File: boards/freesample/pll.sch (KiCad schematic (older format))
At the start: 36 parts, among them J13 SMA, J14 SMA, J22 SMA, J23 SMA, U14 LMK04806, U15 ASG-D-V-A-125.000MHZ

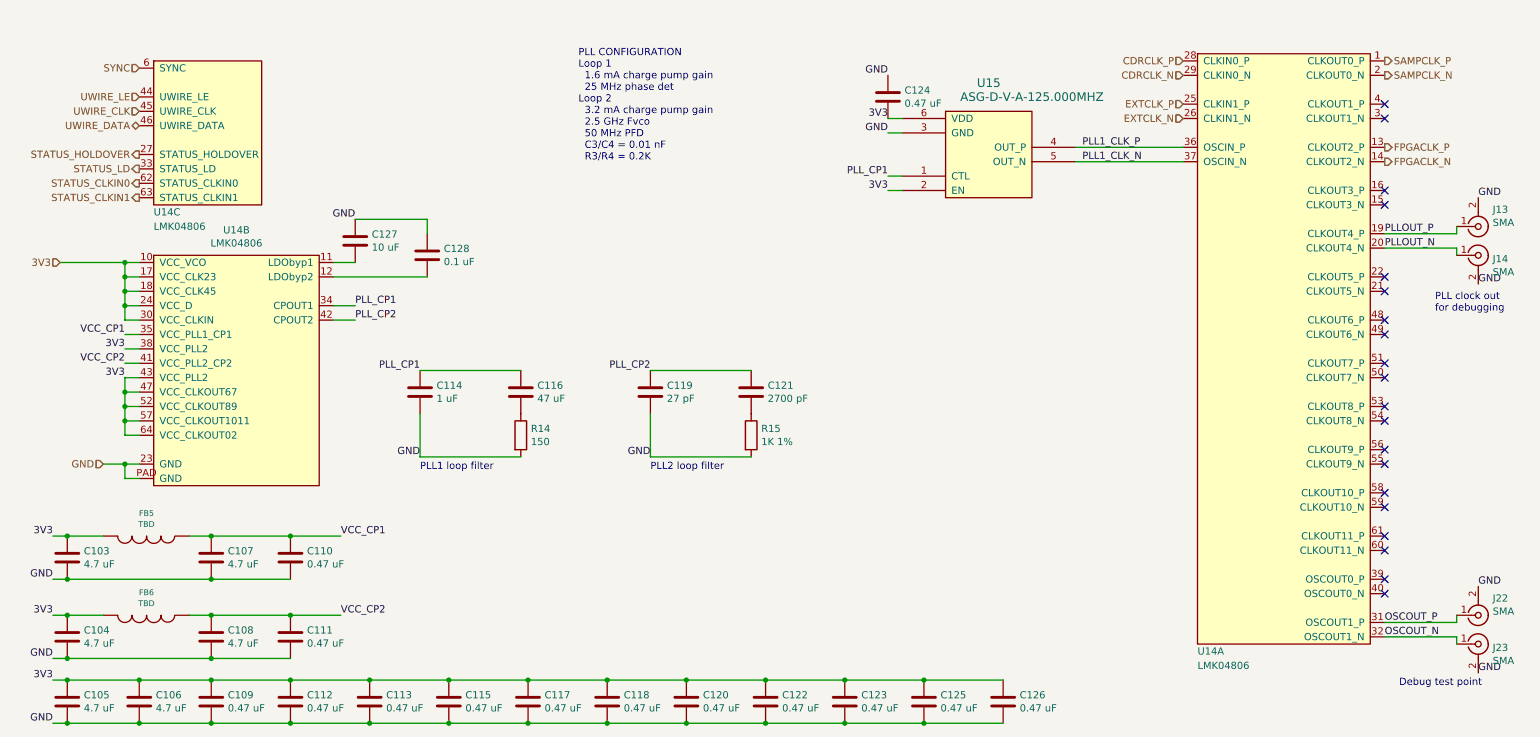
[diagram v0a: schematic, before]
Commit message: Added more test points. Started picking packages for passives. Continued schematic review.
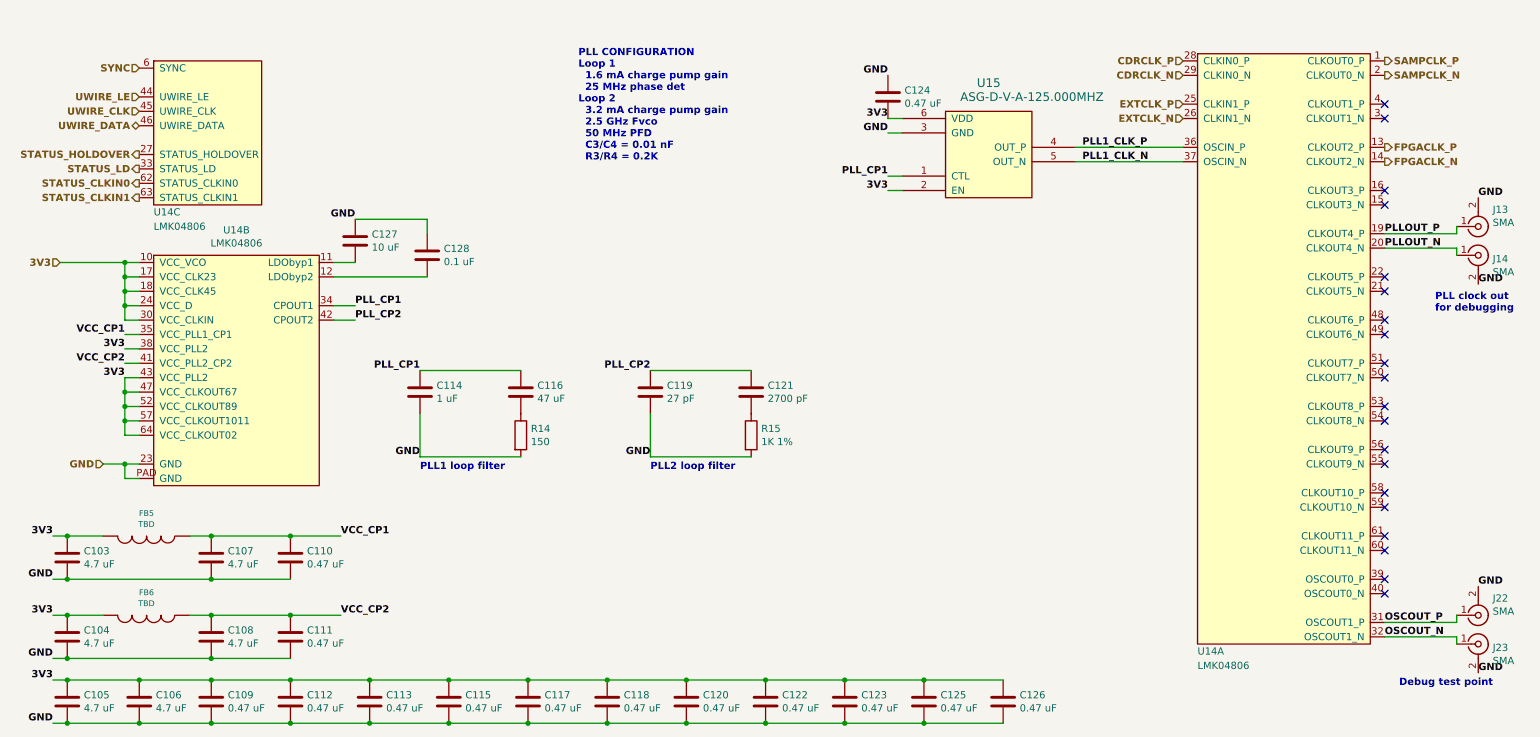
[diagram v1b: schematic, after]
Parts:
- C103, C104, C105, C106, C107, C108: footprint (none) -> azonenberg_pcb:EIA_0603_CAP_NOSILK
- C109, C110, C111, C112, C113, C114, C115, C117, C118, C119, C120, C121, C122, C123, C124, C125, C126, C128: footprint (none) -> azonenberg_pcb:EIA_0402_CAP_NOSILK
- C116: footprint (none) -> azonenberg_pcb:EIA_1210_CAP_NOSILK
- C127: footprint (none) -> azonenberg_pcb:EIA_1206_CAP_NOSILK
- J13, J14, J22, J23: footprint (none) -> azonenberg_pcb:CONN_SMA_EDGE_SAMTEC_SMA_J_P_H_ST_EM1
- U14: footprint (none) -> azonenberg_pcb:QFN_64_0.5MM_9x9MM

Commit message: Continued assigning footprints
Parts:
- FB5, FB6: value TBD -> BLM15PX121SN1D; footprint (none) -> azonenberg_pcb:EIA_0402_CAP_NOSILK
- R14, R15: footprint (none) -> azonenberg_pcb:EIA_0402_RES_NOSILK
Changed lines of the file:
@@
 Sheet 5 12
 Title "FREESAMPLE Oscilloscope"
-Date "2019-03-15"
+Date "2019-03-16"
 Rev "0.1"
 Comp "Andrew D. Zonenberg / Antikernel Labs"
@@
 P 1650 4250
 F 0 "FB5" V 1492 4250 40  0000 C CNN
-F 1 "TBD" V 1568 4250 40  0000 C CNN
-F 2 "" H 1650 4250 60  0001 C CNN
+F 1 "BLM15PX121SN1D" V 1568 4250 40  0000 C CNN
+F 2 "azonenberg_pcb:EIA_0402_CAP_NOSILK" H 1650 4250 60  0001 C CNN
 F 3 "" H 1650 4250 60  0000 C CNN
 	1    1650 4250
@@
 P 1650 4800
 F 0 "FB6" V 1492 4800 40  0000 C CNN
-F 1 "TBD" V 1568 4800 40  0000 C CNN
-F 2 "" H 1650 4800 60  0001 C CNN
+F 1 "BLM15PX121SN1D" V 1568 4800 40  0000 C CNN
+F 2 "azonenberg_pcb:EIA_0402_CAP_NOSILK" H 1650 4800 60  0001 C CNN
 F 3 "" H 1650 4800 60  0000 C CNN
 	1    1650 4800
@@
 F 0 "R14" H 4320 3596 50  0000 L CNN
 F 1 "150" H 4320 3505 50  0000 L CNN
-F 2 "" V 4180 3550 50  0001 C CNN
+F 2 "azonenberg_pcb:EIA_0402_RES_NOSILK" V 4180 3550 50  0001 C CNN
 F 3 "" H 4250 3550 50  0001 C CNN
 	1    4250 3550
@@
 F 0 "R15" H 5920 3596 50  0000 L CNN
 F 1 "1K 1%" H 5920 3505 50  0000 L CNN
-F 2 "" V 5780 3550 50  0001 C CNN
+F 2 "azonenberg_pcb:EIA_0402_RES_NOSILK" V 5780 3550 50  0001 C CNN
 F 3 "" H 5850 3550 50  0001 C CNN
 	1    5850 3550

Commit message: Added fiducials
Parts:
- U15: footprint (none) -> azonenberg_pcb:VCXO_5x7MM_ASG_D
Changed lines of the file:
@@
 F 0 "U15" H 7500 2697 60  0000 C CNN
 F 1 "ASG-D-V-A-125.000MHZ" H 7800 2600 60  0000 C CNN
-F 2 "" H 7200 1900 60  0001 C CNN
+F 2 "azonenberg_pcb:VCXO_5x7MM_ASG_D" H 7200 1900 60  0001 C CNN
 F 3 "" H 7200 1900 60  0000 C CNN
 	1    7200 1900

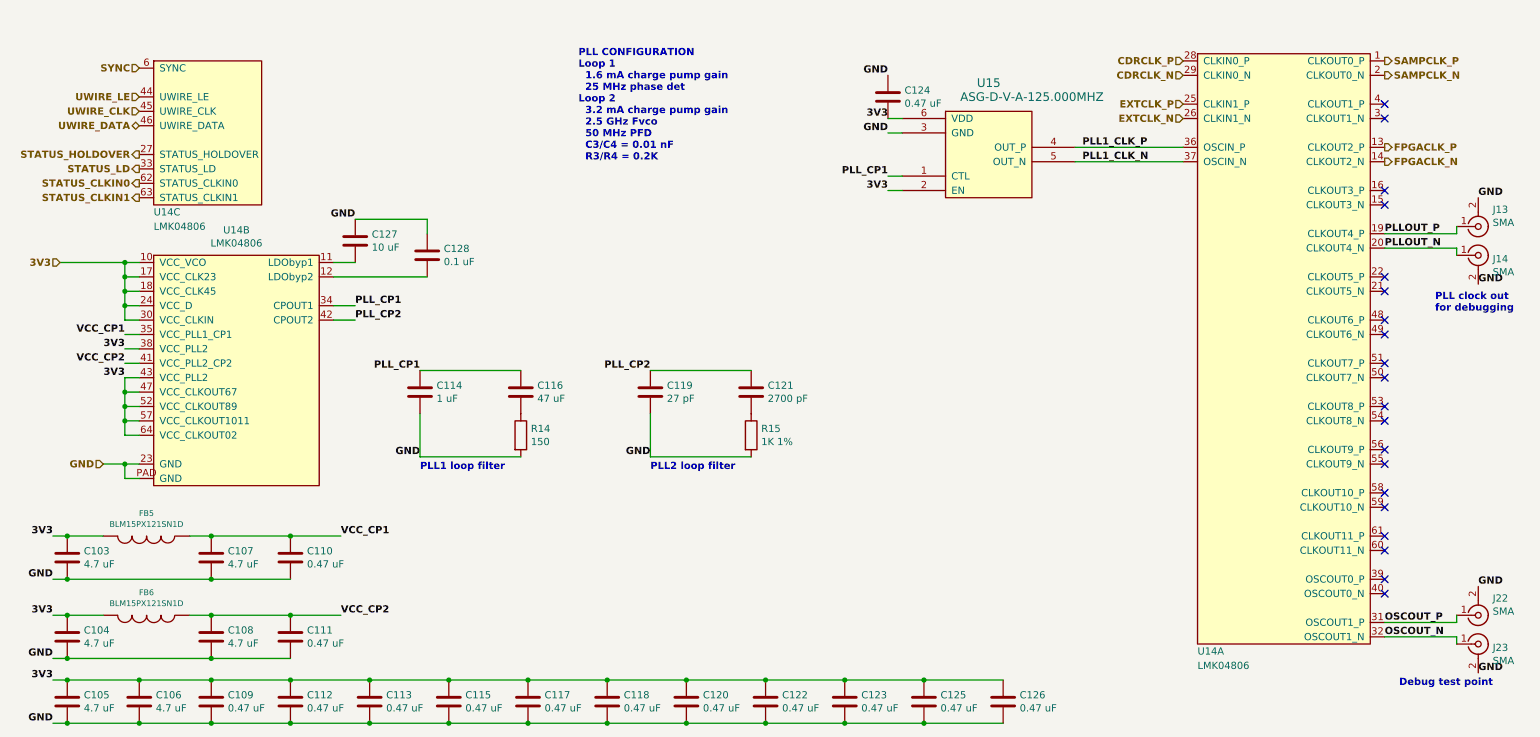
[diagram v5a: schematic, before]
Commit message: Began layout on clock recovery block
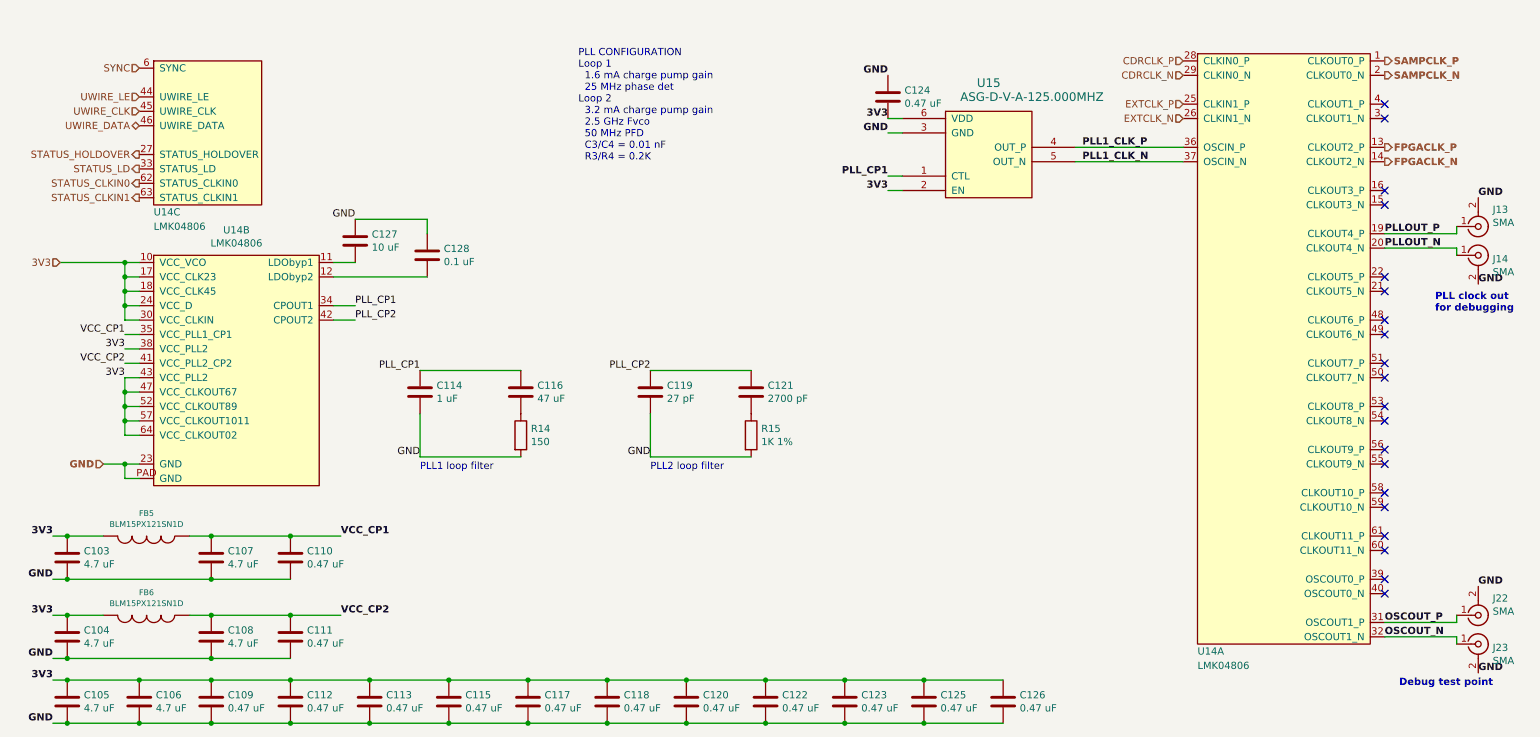
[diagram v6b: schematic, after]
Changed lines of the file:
@@
 Comment4 ""
 $EndDescr
-Text HLabel 8850 950  0    50   Input ~ 10
+Text HLabel 8850 950  0    50   Input ~ 0
 CDRCLK_P
-Text HLabel 8850 1050 0    50   Input ~ 10
+Text HLabel 8850 1050 0    50   Input ~ 0
 CDRCLK_N
-Text HLabel 8850 1250 0    50   Input ~ 10
+Text HLabel 8850 1250 0    50   Input ~ 0
 EXTCLK_P
-Text HLabel 8850 1350 0    50   Input ~ 10
+Text HLabel 8850 1350 0    50   Input ~ 0
 EXTCLK_N
-Text HLabel 1050 2350 0    50   Input ~ 10
+Text HLabel 1050 2350 0    50   Input ~ 0
 3V3
 Text HLabel 1350 3750 0    50   Input ~ 10
@@
 Text HLabel 10250 1050 2    50   Output ~ 10
 SAMPCLK_N
-Text HLabel 1600 1000 0    50   Input ~ 10
+Text HLabel 1600 1000 0    50   Input ~ 0
 SYNC
-Text HLabel 1600 1600 0    50   Output ~ 10
+Text HLabel 1600 1600 0    50   Output ~ 0
 STATUS_HOLDOVER
-Text HLabel 1600 1700 0    50   Output ~ 10
+Text HLabel 1600 1700 0    50   Output ~ 0
 STATUS_LD
-Text HLabel 1600 1200 0    50   Input ~ 10
+Text HLabel 1600 1200 0    50   Input ~ 0
 UWIRE_LE
-Text HLabel 1600 1300 0    50   Input ~ 10
+Text HLabel 1600 1300 0    50   Input ~ 0
 UWIRE_CLK
-Text HLabel 1600 1400 0    50   BiDi ~ 10
+Text HLabel 1600 1400 0    50   BiDi ~ 0
 UWIRE_DATA
-Text HLabel 1600 1800 0    50   Output ~ 10
+Text HLabel 1600 1800 0    50   Output ~ 0
 STATUS_CLKIN0
-Text HLabel 1600 1900 0    50   Output ~ 10
+Text HLabel 1600 1900 0    50   Output ~ 0
 STATUS_CLKIN1
 $Comp
@@
 Wire Wire Line
 	1500 2450 1500 2550
-Text Label 1500 2850 2    50   ~ 10
+Text Label 1500 2850 2    50   ~ 0
 VCC_CP1
 Wire Wire Line
 	1500 2850 1600 2850
-Text Label 1500 3050 2    50   ~ 10
+Text Label 1500 3050 2    50   ~ 0
 VCC_CP2
 Wire Wire Line
 	1500 3050 1600 3050
-Text Label 1500 2950 2    50   ~ 10
+Text Label 1500 2950 2    50   ~ 0
 3V3
 Wire Wire Line
 	1500 2950 1600 2950
-Text Label 1500 3150 2    50   ~ 10
+Text Label 1500 3150 2    50   ~ 0
 3V3
 Wire Wire Line
@@
 NoConn ~ 10250 4550
 NoConn ~ 10250 4650
-Text Label 3100 2650 0    50   ~ 10
+Text Label 3100 2650 0    50   ~ 0
 PLL_CP1
 Wire Wire Line
 	3100 2650 2950 2650
-Text Label 3550 3100 2    50   ~ 10
-PLL_CP1
-Text Label 3550 3700 2    50   ~ 10
+Text Label 3550 3700 2    50   ~ 0
 GND
 $Comp
@@
 Wire Wire Line
 	3550 3100 4250 3100
-Text Notes 3550 3800 0    50   ~ 10
-PLL1 loop filter
 $Comp
 L device:C C119
@@
 	1    0    0    -1
 $EndComp
-Text Label 5150 3100 2    50   ~ 10
-PLL_CP2
-Text Label 5150 3700 2    50   ~ 10
-GND
 $Comp
 L device:C C121
@@
 Wire Wire Line
 	5150 3100 5850 3100
-Text Notes 5150 3800 0    50   ~ 10
-PLL2 loop filter
 $Comp
 L osc-azonenberg:OSC_LVDS_VCXO U15
@@
 Text Label 6800 1050 2    50   ~ 10
 GND
-Text Label 3100 2750 0    50   ~ 10
+Text Label 3100 2750 0    50   ~ 0
 PLL_CP2
 Wire Wire Line
@@
 Wire Wire Line
 	2950 2350 3100 2350
-Text Label 3100 2050 2    50   ~ 10
-GND
 $Comp
 L device:C C128
@@
 Wire Wire Line
 	3600 2050 3600 2150
-Text Notes 4650 1650 0    50   ~ 10
+Text Notes 4650 1650 0    50   ~ 0
 PLL CONFIGURATION\nLoop 1\n  1.6 mA charge pump gain\n  25 MHz phase det\nLoop 2\n  3.2 mA charge pump gain\n  2.5 GHz Fvco\n  50 MHz PFD\n  C3/C4 = 0.01 nF\n  R3/R4 = 0.2K
 $Comp
@@
 Text Notes 10350 5300 0    50   ~ 10
 Debug test point
+Text Label 5150 3700 2    50   ~ 0
+GND
+Text Label 5150 3100 2    50   ~ 0
+PLL_CP2
+Text Notes 5150 3800 0    50   ~ 0
+PLL2 loop filter
+Text Notes 3550 3800 0    50   ~ 0
+PLL1 loop filter
+Text Label 3100 2050 2    50   ~ 0
+GND
+Text Label 3550 3100 2    50   ~ 0
+PLL_CP1
 $EndSCHEMATC
